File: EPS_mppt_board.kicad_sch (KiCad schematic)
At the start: 0 parts

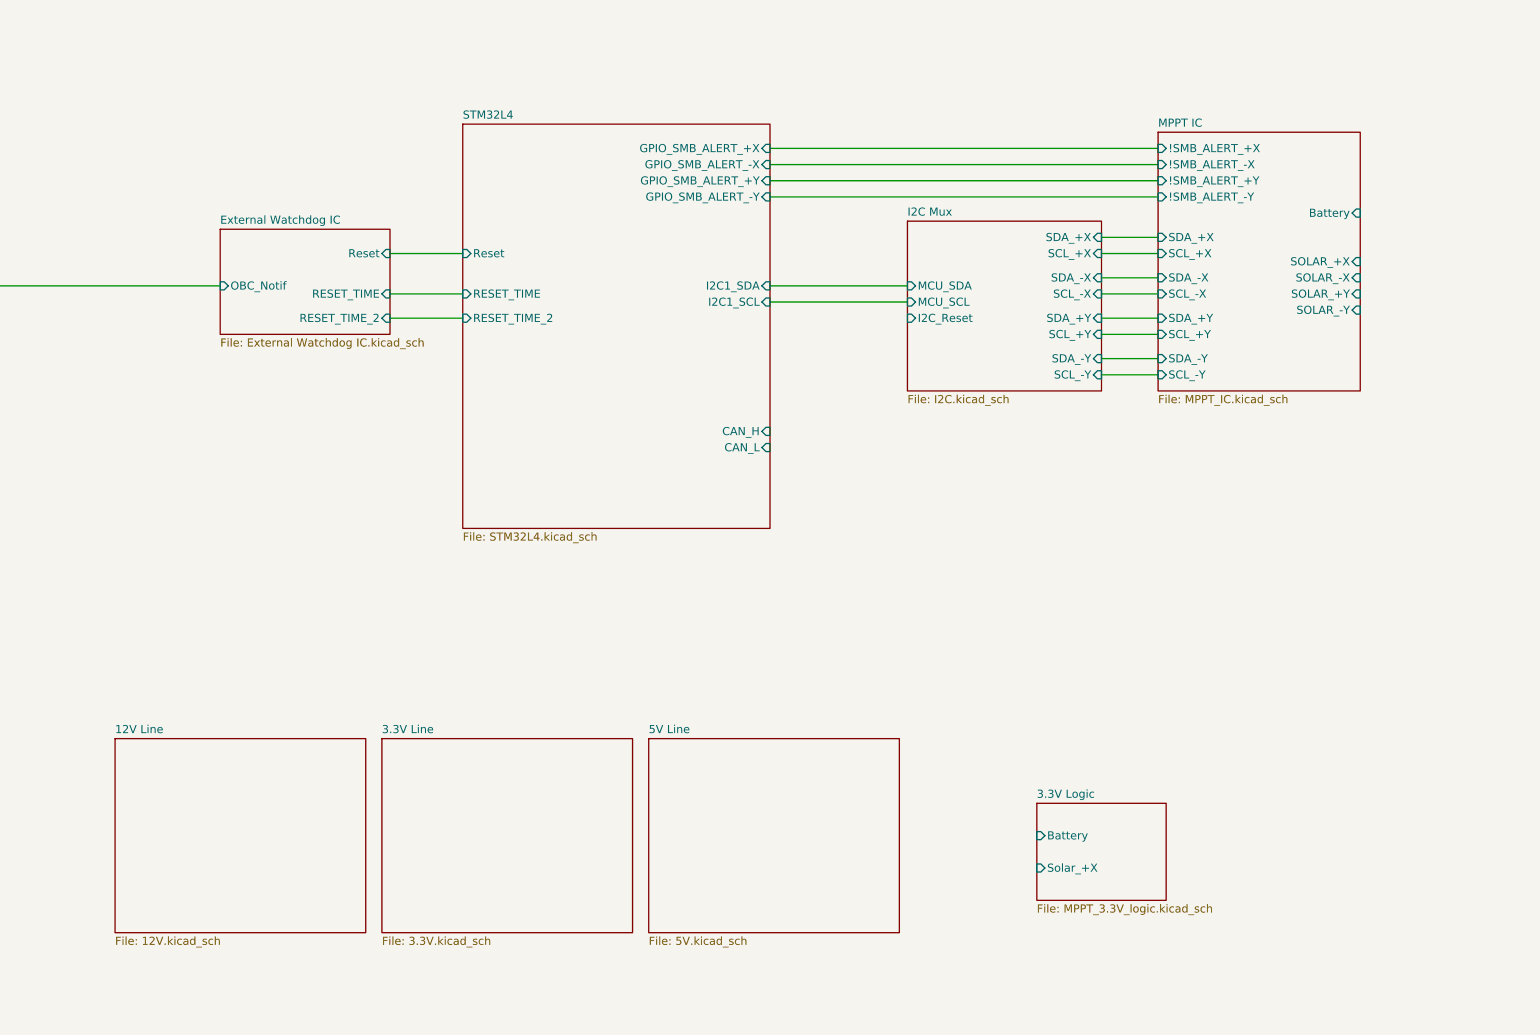
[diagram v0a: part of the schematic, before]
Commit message: Added 3.3V and 12V lines
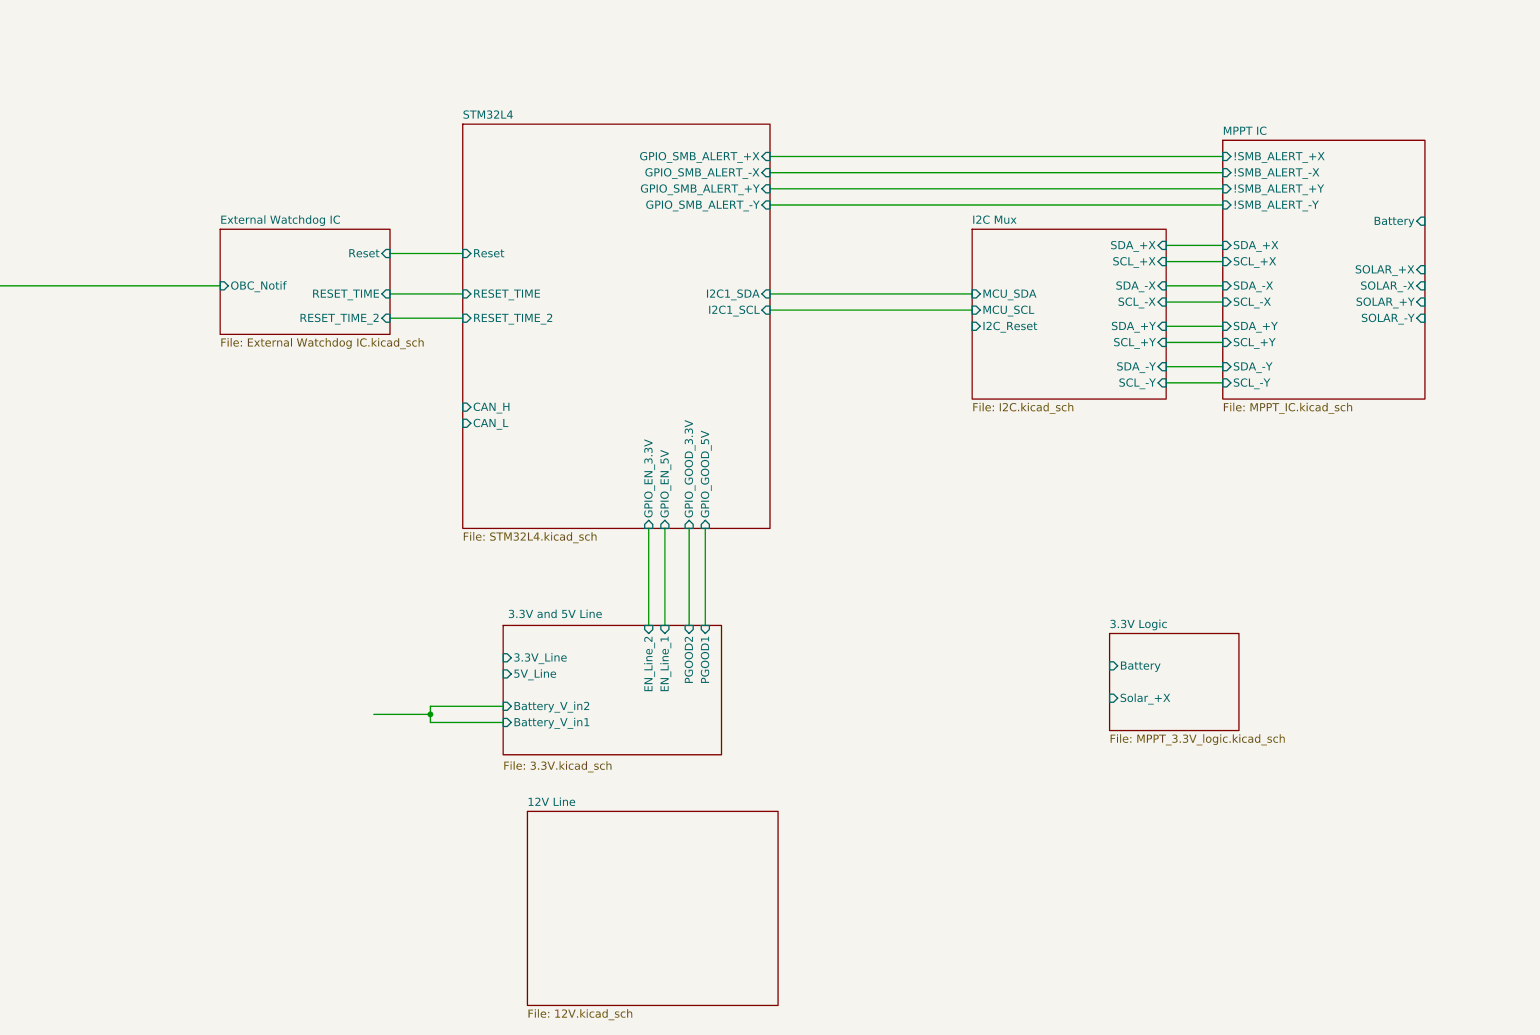
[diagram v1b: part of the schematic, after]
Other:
- sheet 3.3V Line renamed 3.3V and 5V Line
- removed sheet 5V Line
- sheet 3.3V and 5V Line ports: added 3.3V_Line, 5V_Line, Battery_V_in1, Battery_V_in2, EN_Line_1, EN_Line_2, PGOOD1, PGOOD2; removed none
- sheet STM32L4 ports: added GPIO_EN_3.3V, GPIO_EN_5V, GPIO_GOOD_3.3V, GPIO_GOOD_5V; removed none

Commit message: Added cap to output of lines
based on LTSpice Simulation
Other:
- removed sheet 12V Line
- removed sheet External WatchDog
- removed sheet MPPT
- removed sheet STM32
- added sheet Current Sensing and Fault Detection (Sensing.kicad_sch)
- sheet STM32L4 ports: added I2C_Mult_RESET; removed none
- company: (none) -> QSET (Jaron Cyna)

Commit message: added current sensing and e-fuses
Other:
- sheet Current Sensing and Fault Detection ports: added 3V3_Line, 5V_Line, ADCS_3V3_ShutDown, ADCS_5V_ShutDown, CRIT_INA3221, OBC_3V3_ShutDown, PV_INA3221, SCL_INA3221, SDA_INA3221, WAR_INA3221; removed none
- sheet STM32L4 ports: added ADCS_3V3_SD, ADCS_5V_SD, OBC_3V3_SD; removed none
- note added: "Board Power"
- note added: "Connectivity"
- note added: "MCU"
- note added: "MPPT"
- note added: "Saftey"
